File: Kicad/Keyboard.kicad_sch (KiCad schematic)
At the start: 18 parts, among them J1 USB_C_Receptacle_USB2.0_16P, J2 Conn_01x04, SW1 SW_Push, U1 ATmega32U4-A, U2 USB6B1, Y1 Crystal_GND24_Small

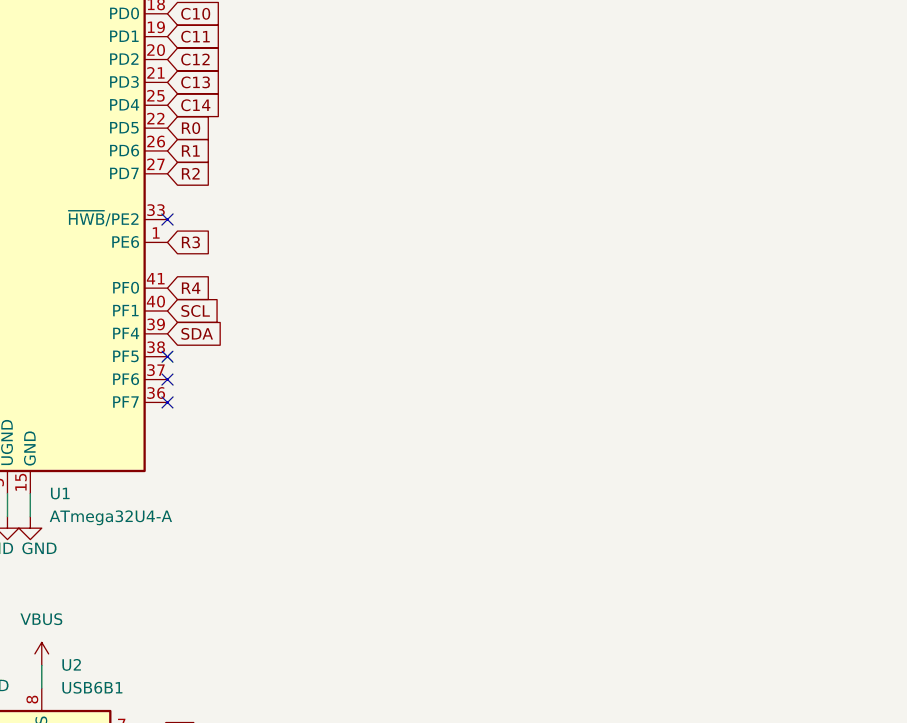
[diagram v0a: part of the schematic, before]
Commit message: add encoder + hardware debouncing
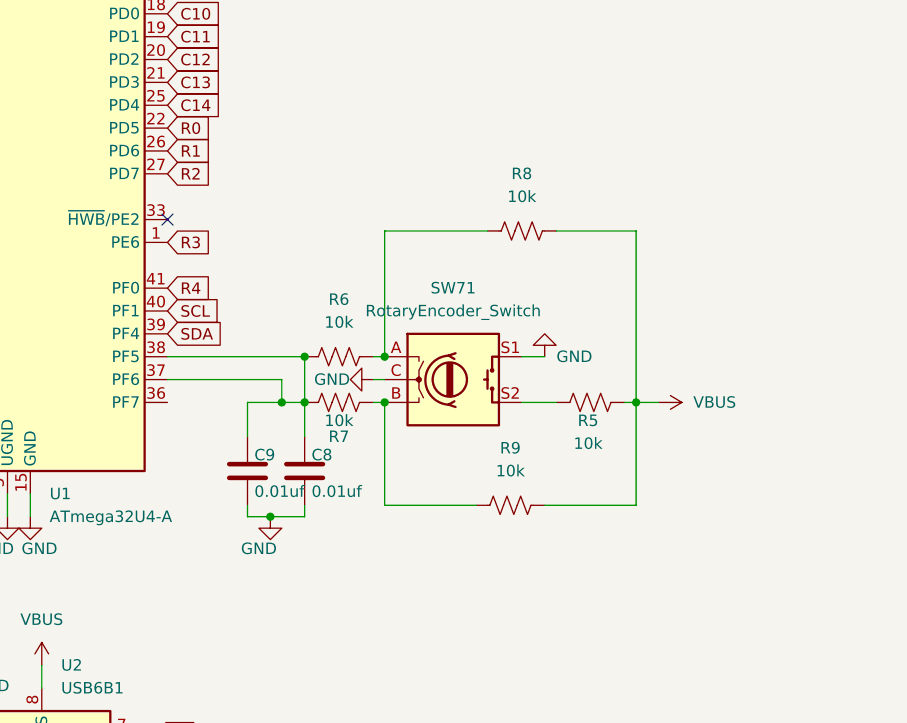
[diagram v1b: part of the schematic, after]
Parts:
- added C8, C9: 0.01uf, Capacitor_SMD:C_01005_0402Metric_Pad0.57x0.30mm_HandSolder, symbol Device:C
- added R5, R6, R7, R8, R9: 10k, Resistor_SMD:R_0402_1005Metric_Pad0.72x0.64mm_HandSolder, symbol Device:R_US
- added SW71: RotaryEncoder_Switch, Rotary_Encoder:RotaryEncoder_Bourns_Vertical_PEL12D-4xxxF-Sxxxx, symbol Device:RotaryEncoder_Switch
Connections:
- net GND: now also C8.2, C9.2, SW71.C, SW71.S1
- net VBUS: now also R5.2, R8.2, R9.2
- net at U1.37 (PF6): now also U1.38 (PF5), C8.1, C9.1, R6.1, R7.1
- new net: R7.2, R9.1, SW71.B
- new net: R6.2, R8.1, SW71.A
- new net: R5.1, SW71.S2
- no-connect marks 7 -> 4

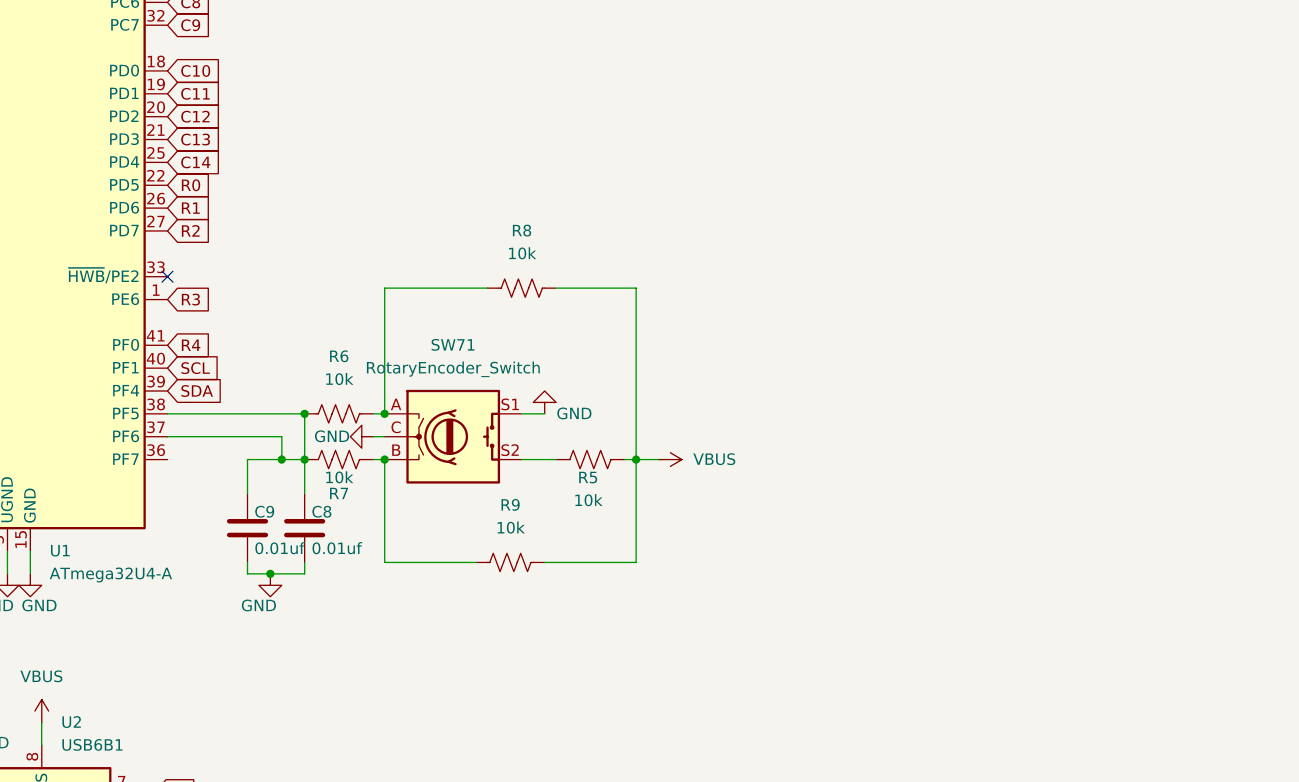
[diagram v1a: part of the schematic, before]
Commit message: added bootloader
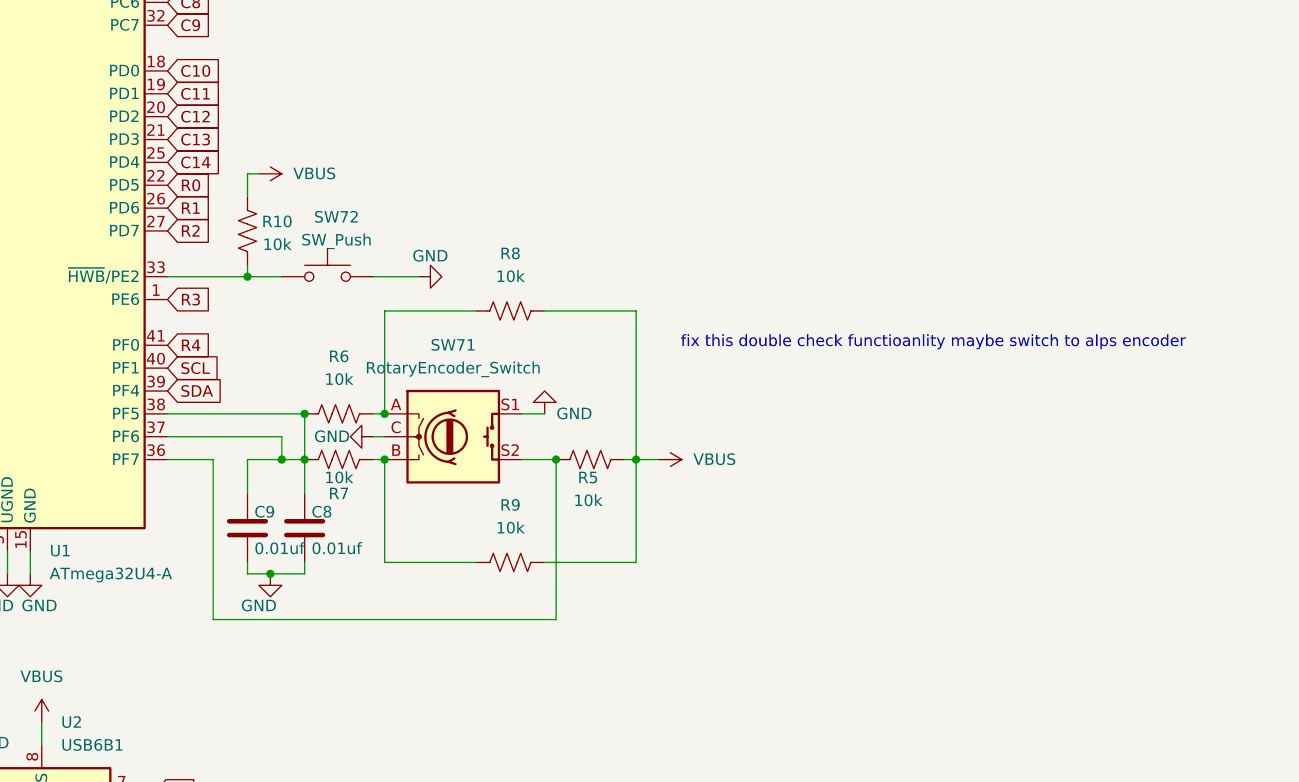
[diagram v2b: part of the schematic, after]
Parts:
- added R10: 10k, Resistor_SMD:R_0402_1005Metric_Pad0.72x0.64mm_HandSolder, symbol Device:R_US
- added SW72: SW_Push, Button_Switch_SMD:SW_Tactile_SPST_NO_Straight_CK_PTS636Sx25SMTRLFS, symbol Switch:SW_Push
- SW71: footprint Rotary_Encoder:RotaryEncoder_Bourns_Vertical_PEL12D-4xxxF-Sxxxx -> Rotary_Encoder:RotaryEncoder_Alps_EC11E-Switch_Vertical_H20mm_CircularMountingHoles
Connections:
- net GND: now also SW72.2
- net VBUS: now also R10.1
- net at R5.1, SW71.S2: now also U1.36 (PF7)
- net at U1.33 (~{HWB}/PE2): now also R10.2, SW72.1
- no-connect marks 4 -> 3
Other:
- note added: "fix this double check functioanlity maybe switch to alps encoder"
- moved on the sheet: R8

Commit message: cancer traces
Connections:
- net at C8.1, R6.1, U1.38 (PF5): no longer C9.1, R7.1, U1.37 (PF6)
- new net: C9.1, R7.1, U1.37 (PF6)
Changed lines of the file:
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@@
+	)
+	(junction
+		(at 91.44 106.68)
+		(diameter 0)
+		(color 0 0 0 0)
 	)
 	(junction
@@
 	)
 	(junction
-		(at 92.71 111.76)
-		(diameter 0)
-		(color 0 0 0 0)
-	)
-	(junction
 		(at 59.69 29.21)
 		(diameter 0)
@@
 	(junction
 		(at 33.02 49.53)
-		(diameter 0)
-		(color 0 0 0 0)
-	)
-	(junction
-		(at 92.71 106.68)
 		(diameter 0)
 		(color 0 0 0 0)
@@
 	(wire
 		(pts
+			(xy 92.71 115.57) (xy 92.71 114.3)
+		)
+		(stroke
+			(width 0)
+			(type default)
+		)
+	)
+	(wire
+		(pts
 			(xy 45.72 153.67) (xy 53.34 153.67)
 		)
@@
 	(wire
 		(pts
-			(xy 77.47 106.68) (xy 92.71 106.68)
+			(xy 77.47 106.68) (xy 91.44 106.68)
 		)
 		(stroke
@@
 	(wire
 		(pts
-			(xy 92.71 111.76) (xy 92.71 115.57)
+			(xy 92.71 114.3) (xy 91.44 114.3)
 		)
 		(stroke
@@
 	(wire
 		(pts
-			(xy 92.71 106.68) (xy 92.71 111.76)
-		)
-		(stroke
-			(width 0)
-			(type default)
-		)
-	)
-	(wire
-		(pts
 			(xy 119.38 95.25) (xy 129.54 95.25)
 		)
@@
 	(wire
 		(pts
+			(xy 91.44 106.68) (xy 92.71 106.68)
+		)
+		(stroke
+			(width 0)
+			(type default)
+		)
+	)
+	(wire
+		(pts
 			(xy 71.12 15.24) (xy 71.12 17.78)
 		)
@@
 		)
 		(stroke
+			(width 0)
+			(type default)
+		)
+	)
+	(wire
+		(pts
+			(xy 91.44 106.68) (xy 91.44 114.3)
+		)
+		(stroke

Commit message: updated bootloader and reset footprints + symbols + reroute traces
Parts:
- removed SW1, SW72: SW_Push, Button_Switch_SMD:SW_Tactile_SPST_NO_Straight_CK_PTS636Sx25SMTRLFS, symbol Switch:SW_Push
- added SW1, SW72: ~, a:Pushbuttonthing, symbol New_Symbols:Pushbuttonthing
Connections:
- net GND: now also SW1.1, SW72.2
- net at 10k1.2, U1.13 (~{RESET}): now also SW1.4
- net at R10.2, U1.33 (~{HWB}/PE2): now also SW72.3
- no-connect marks 3 -> 11

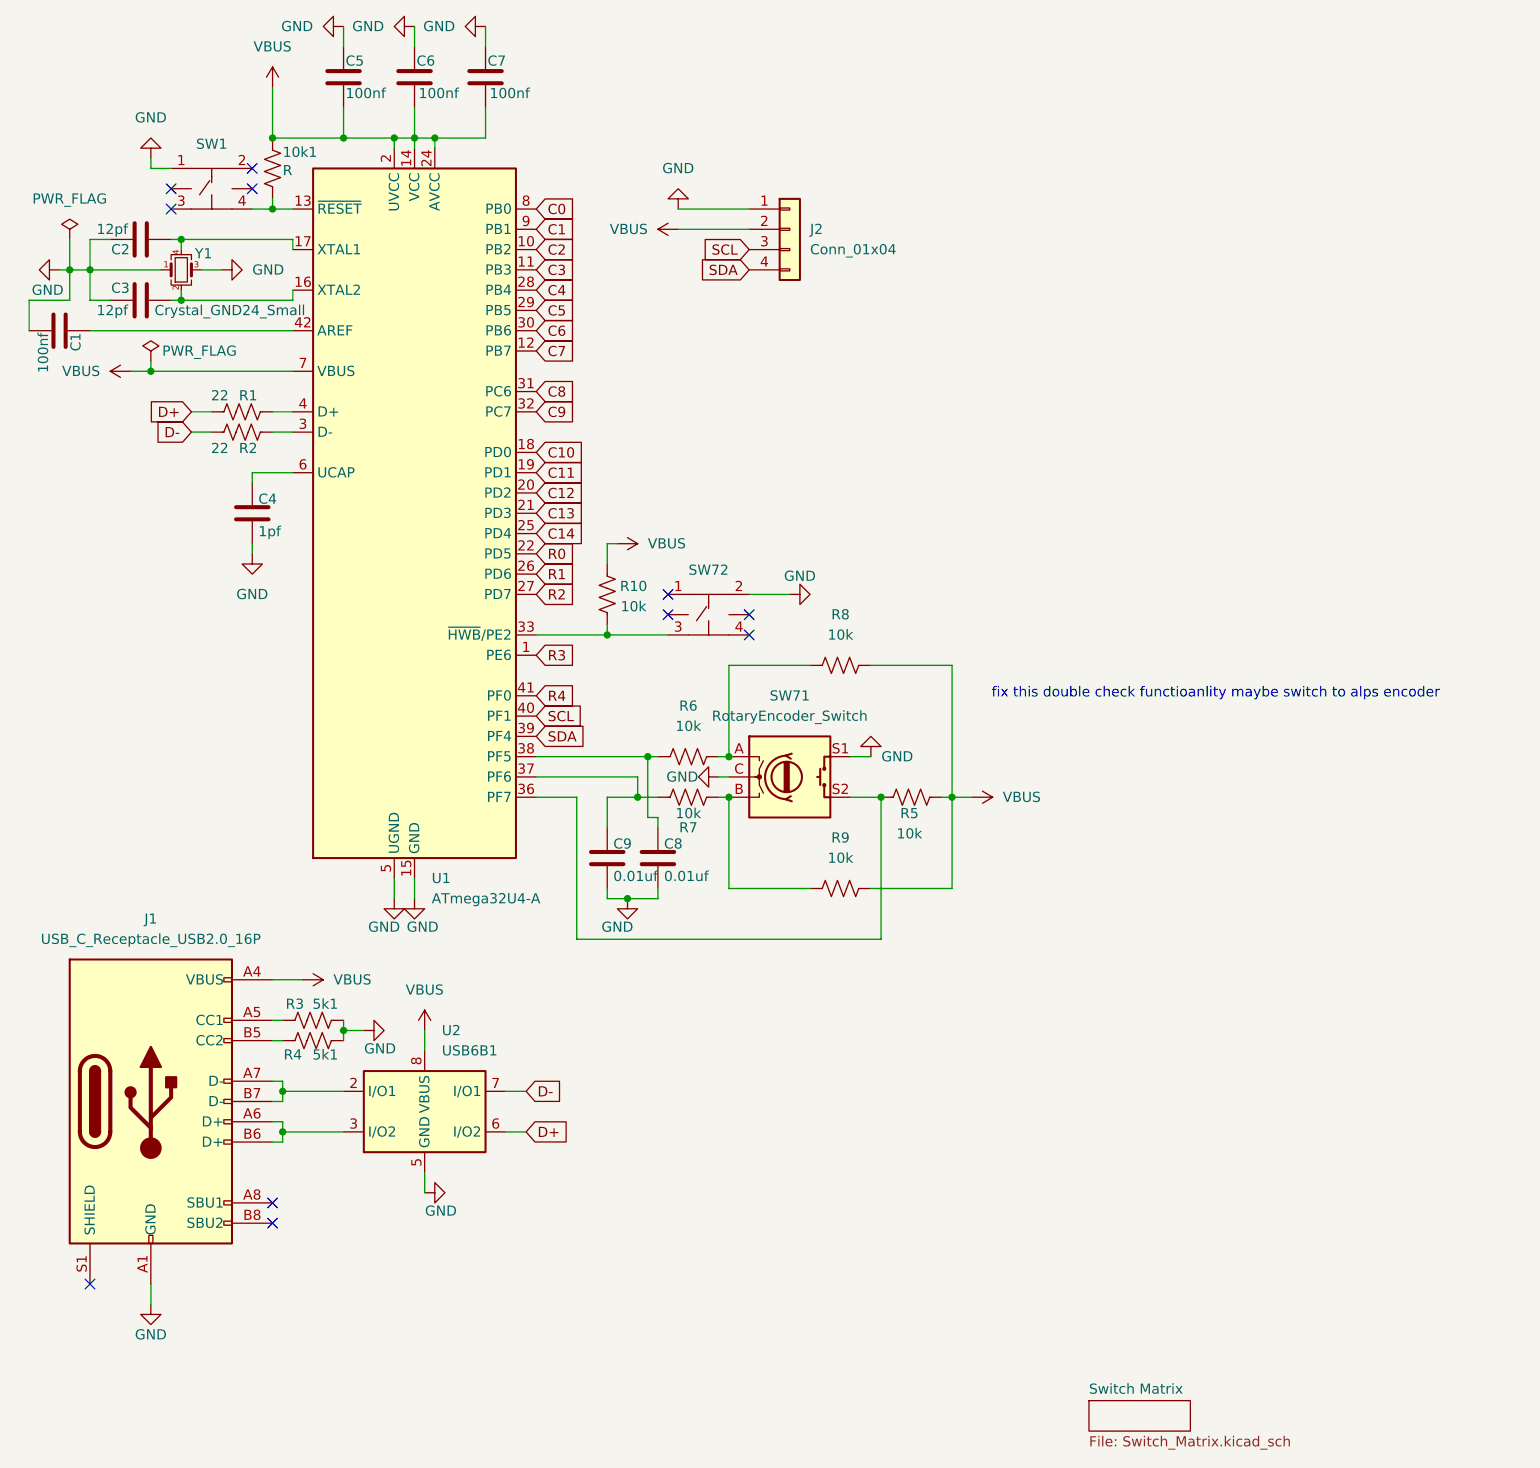
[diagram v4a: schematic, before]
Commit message: differential routing + board review
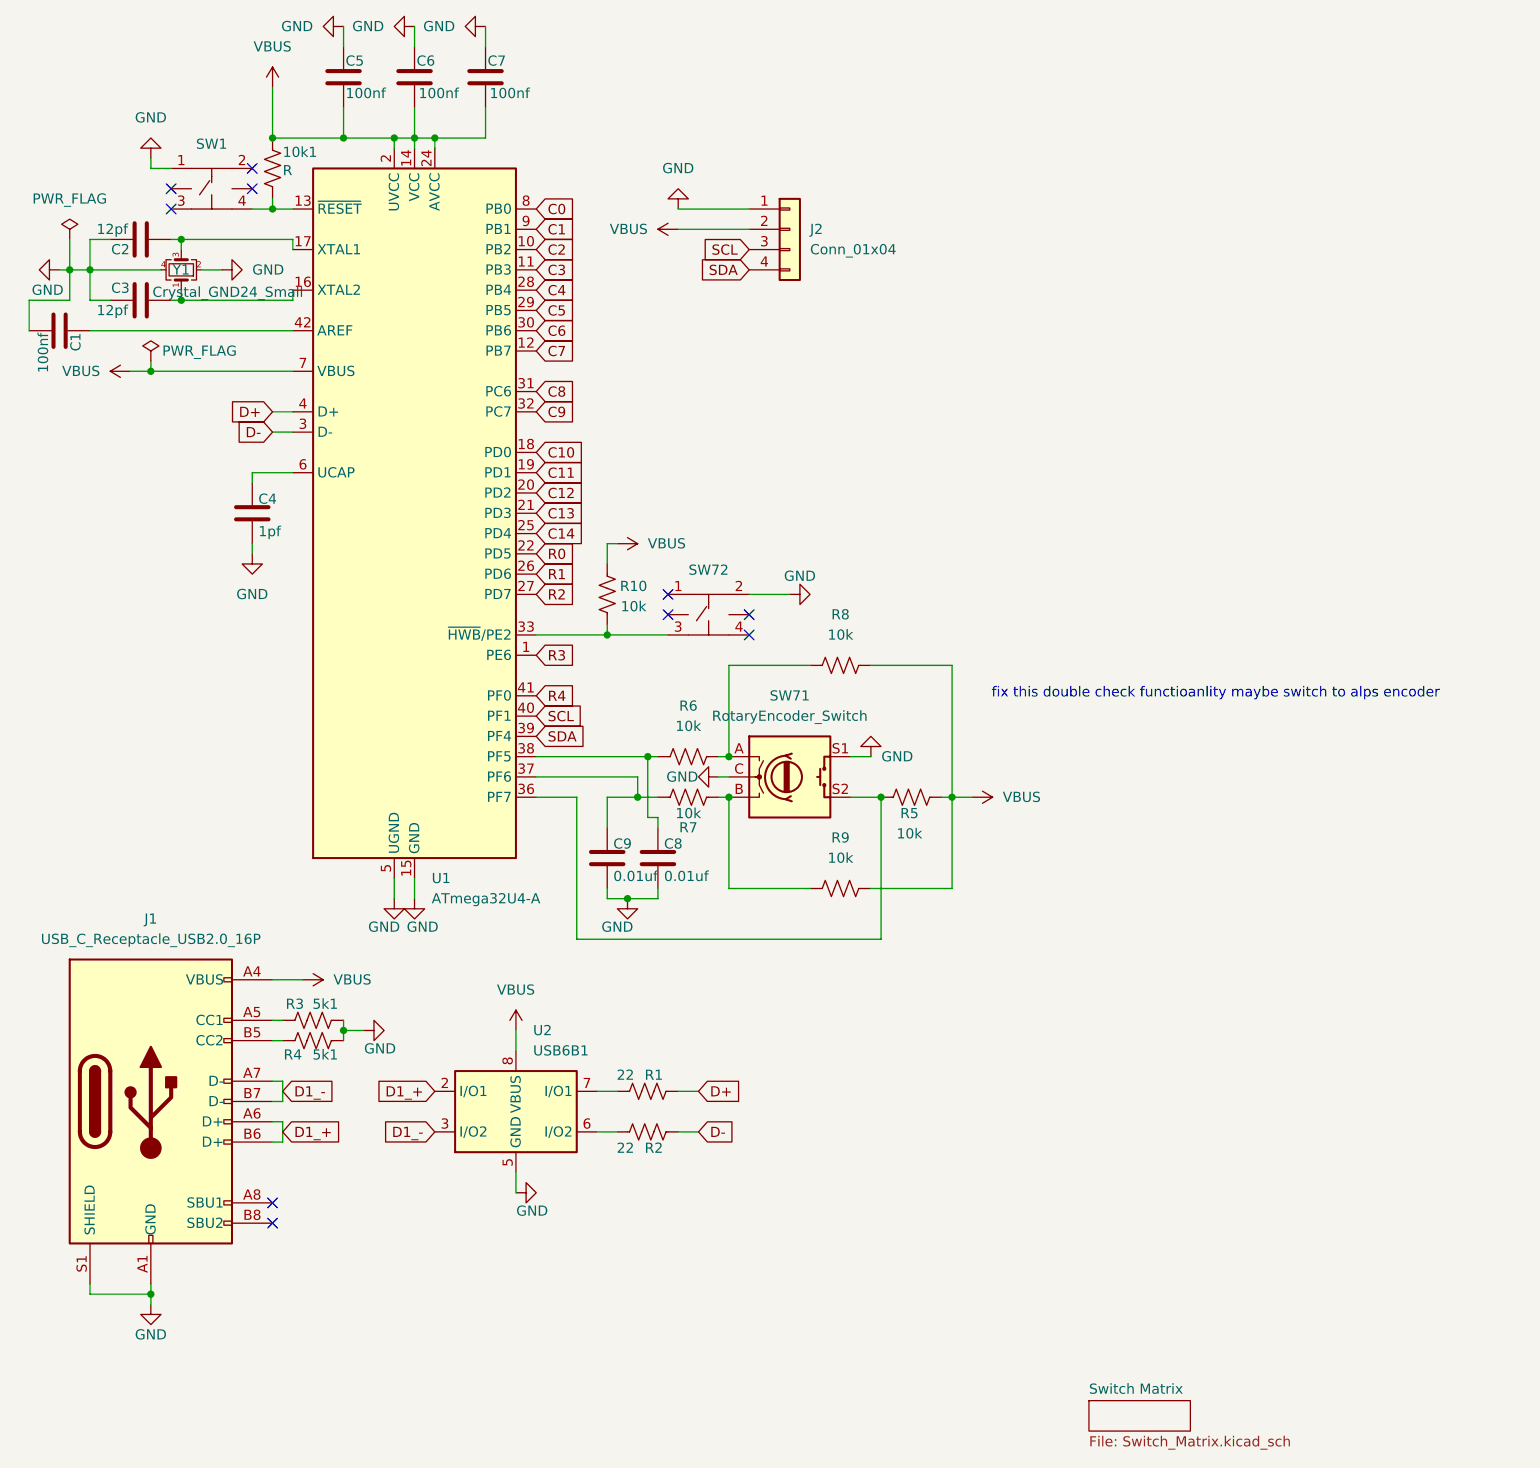
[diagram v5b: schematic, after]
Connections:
- net D+: now also R1.2, U1.4 (D+); no longer R1.1, U2.6 (I/O2)
- net D-: now also R2.1, U1.3 (D-); no longer R2.2, U2.7 (I/O1)
- net GND: now also J1.S1 (SHIELD), Y1.2, Y1.4; no longer Y1.1, Y1.3
- net at C2.1, U1.17 (XTAL1): now also Y1.3; no longer Y1.4
- net D1_+: now reaches J1.A6 (D+), J1.B6 (D+)
- net D1_+: now also U2.2 (I/O1); no longer U2.3 (I/O2)
- net D1_-: now reaches J1.A7 (D-), J1.B7 (D-)
- net D1_-: now also U2.3 (I/O2); no longer U2.2 (I/O1)
- net at C3.1, U1.16 (XTAL2): now also Y1.1; no longer Y1.2
- new net: R2.2, U2.6 (I/O2)
- new net: R1.1, U2.7 (I/O1)
- no-connect marks 11 -> 10
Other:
- moved on the sheet: R1, R2, U2, Y1

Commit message: fix mounting holes finalizing stuff
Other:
- note removed: "fix this double check functioanlity maybe switch to alps encoder"
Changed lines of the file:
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@@
 		(comment 1 "65% keyboard")
-	)
-	(text "fix this double check functioanlity maybe switch to alps encoder"
-		(exclude_from_sim no)
-		(at 162.56 98.806 0)
-		(effects
-			(font
-				(size 1.27 1.27)
-			)
-		)
 	)
 	(junction
